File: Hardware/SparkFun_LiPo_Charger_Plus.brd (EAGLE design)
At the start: 38.1 x 14 mm, 35 parts, among them U1 MCP73833

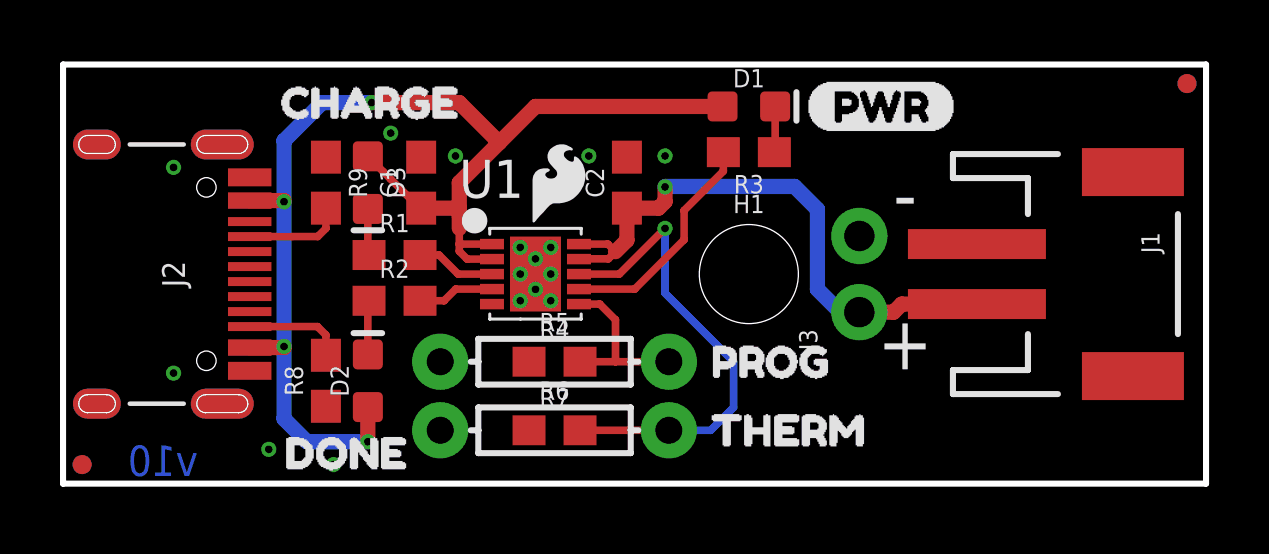
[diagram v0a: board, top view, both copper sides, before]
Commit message: v10 Update
Added PROD_ID to U1, fixed part number ordering.
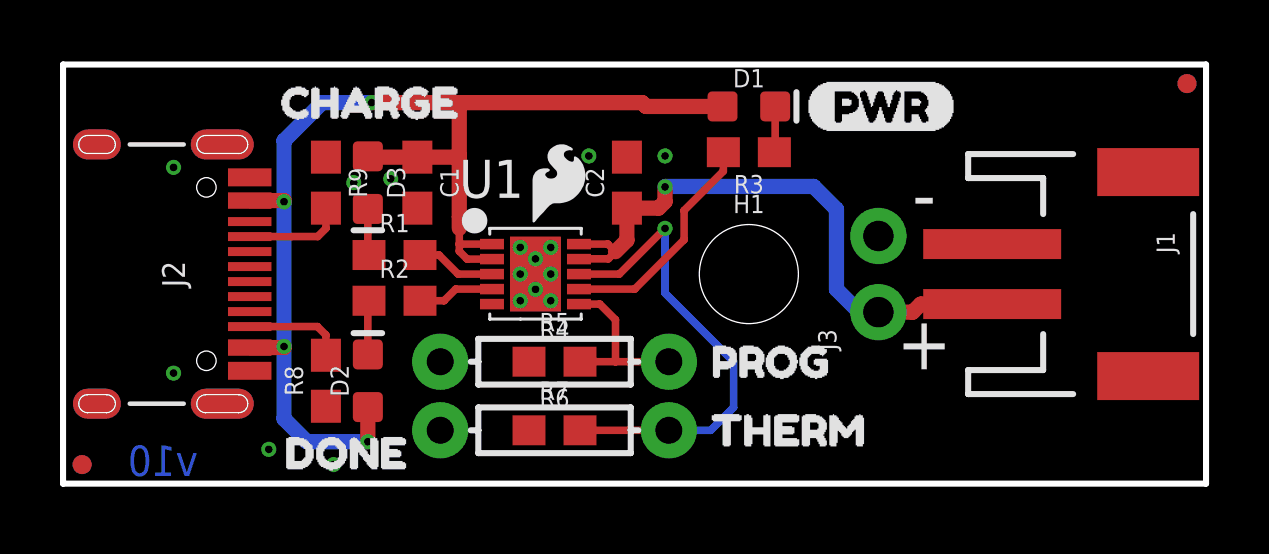
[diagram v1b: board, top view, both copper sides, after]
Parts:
- R6: value THERM -> 10k; device SparkFun-Resistors:AXIAL-0.3 -> SparkFun-Resistors:0603
- R7: value 10k -> THERM; device SparkFun-Resistors:0603 -> SparkFun-Resistors:AXIAL-0.3
- moved J3 0.64 mm to (27.2, 5.71)
- moved J1 0.51 mm to (34.7, 6.99)
- moved C1 0.13 mm to (11.8, 10.0), turned to 270 degrees
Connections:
- net GND: now also R6.1, R7.P$1; no longer R6.P$1, R7.1
- net THERM: now also R6.2, R7.P$2; no longer R6.P$2, R7.2
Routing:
- net VDD: track 42.3 -> 41.6 mm
- net V_BATT: track 19.9 -> 20.4 mm

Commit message: QC Fixes
Adjusted bottom silk
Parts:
- moved U$9 1.91 mm to (36.1, 14.0)
- moved LOGO1 1.27 mm to (32.6, 6.99)
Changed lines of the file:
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@@
 <element name="U$6" library="buzzard_labels (14)" package="THERM8" value="" x="20.701" y="1.778"/>
 <element name="U$7" library="buzzard_labels (14)" package="PWR6" value="" x="24.765" y="12.573"/>
-<element name="LOGO1" library="SparkFun-Aesthetics" package="SFE_LOGO_NAME_FLAME_.1" value="SFE_LOGO_NAME_FLAME.1_INCH" x="31.369" y="6.985" rot="MR270"/>
+<element name="LOGO1" library="SparkFun-Aesthetics" package="SFE_LOGO_NAME_FLAME_.1" value="SFE_LOGO_NAME_FLAME.1_INCH" x="32.639" y="6.985" rot="MR270"/>
 <element name="LOGO2" library="SparkFun-Aesthetics" package="OSHW-LOGO-S" value="OSHW-LOGOS" x="2.921" y="6.985" rot="MR270"/>
 <element name="U$1" library="SparkFun-Aesthetics" package="SFE_LOGO_FLAME_.1" value="" x="16.51" y="10.033"/>
@@
 <attribute name="REV" value="" x="-1.905" y="-24.13" size="1.016" layer="27" font="vector" ratio="15" display="off"/>
 </element>
-<element name="U$9" library="buzzard_labels (15)" package="LIPO_CHARGER_PLUS0" value="" x="34.163" y="13.97" rot="MR270"/>
+<element name="U$9" library="buzzard_labels (15)" package="LIPO_CHARGER_PLUS0" value="" x="36.068" y="13.97" rot="MR270"/>
 </elements>
 <signals>
